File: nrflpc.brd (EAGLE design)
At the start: 67.9 x 38.8 mm, 62 parts, among them IC1 LPC1111/12/13/14-HVQFN33, IC3 LM3401, IC5 LM3401, IC6 LM3401, IC7 LM3401, IC8 78L05SMD, Q1 20MHz, Q2 MOSFET-PCHANNEL, Q3 MOSFET-PCHANNEL, Q4 MOSFET-PCHANNEL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

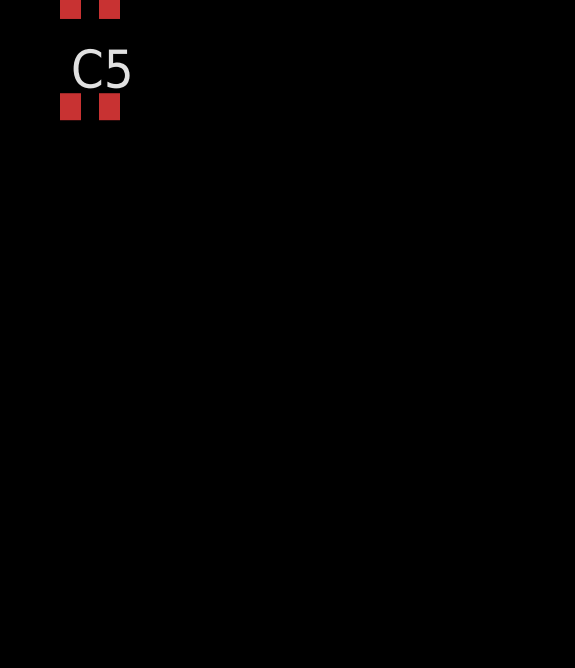
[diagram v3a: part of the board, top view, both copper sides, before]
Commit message: ADC input filters
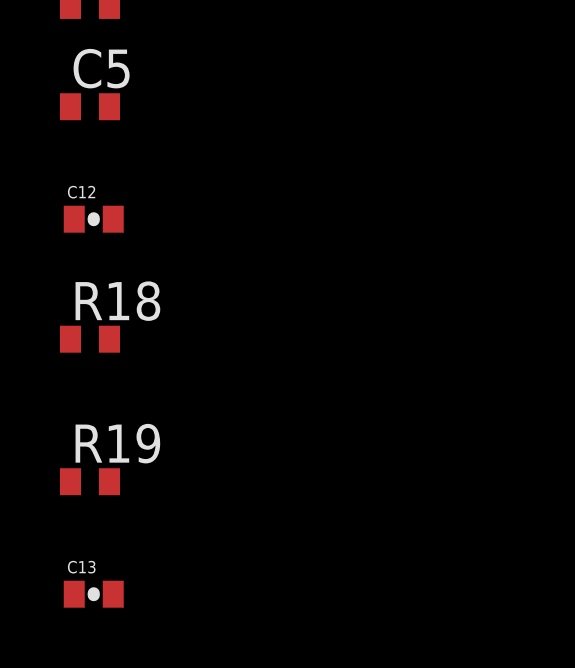
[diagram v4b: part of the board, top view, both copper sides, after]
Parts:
- added C12, C13: 200pF, SparkFun:0402-CAP
- added R18, R19: 4.7k, rcl:R0402
- R1: value (none) -> 100k
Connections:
- removed net AD0: IC1.20
- new net AD6: C13.2, IC1.20, R19.2
- new net AIN0: R18.1
- new net AIN1: R19.1
- net AD1: now also C12.2, R18.2
- net GND: now also C12.1, C13.1
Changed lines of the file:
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@@
 <element name="C3" library="rcl" package="C0402" value="100nF" x="-8.875" y="-15.125"/>
 <element name="C4" library="rcl" package="C0402" value="100nF" x="-8.875" y="-18.5"/>
-<element name="R1" library="rcl" package="R0402" value="" x="-8.875" y="-23.25"/>
+<element name="R1" library="rcl" package="R0402" value="100k" x="-8.875" y="-23.25"/>
 <element name="C5" library="rcl" package="C0402" value="100nF" x="-8.875" y="-26.625"/>
 <element name="PWR" library="pinhead" package="1X02" value="" x="11.375" y="2.75"/>
+<element name="C12" library="SparkFun" package="0402-CAP" value="200pF" x="-8.75" y="-30.375"/>
+<element name="R18" library="rcl" package="R0402" value="4.7k" x="-8.875" y="-34.375"/>
+<element name="C13" library="SparkFun" package="0402-CAP" value="200pF" x="-8.75" y="-42.875"/>
+<element name="R19" library="rcl" package="R0402" value="4.7k" x="-8.875" y="-39.125"/>
 </elements>
 <signals>
@@
 <contactref element="C5" pad="2"/>
 <contactref element="PWR" pad="2"/>
-<wire x1="34.549" y1="19.0205" x2="32.625" y2="8.75" width="0" layer="19" extent="1-1"/>
+<contactref element="C12" pad="1"/>
+<contactref element="C13" pad="1"/>
+<wire x1="52.178" y1="32.8" x2="57.66" y2="33.496" width="0" layer="19" extent="1-1"/>
+<wire x1="50.252" y1="32.743" x2="52.178" y2="32.8" width="0" layer="19" extent="1-1"/>
+<wire x1="49.752" y1="31.143" x2="50.252" y2="32.743" width="0" layer="19" extent="1-1"/>
+<wire x1="48.352" y1="30.743" x2="49.752" y2="31.143" width="0" layer="19" extent="1-1"/>
+<wire x1="48.152" y1="29.243" x2="48.352" y2="30.743" width="0" layer="19" extent="1-1"/>
+<wire x1="49.752" y1="29.343" x2="48.152" y2="29.243" width="0" layer="19" extent="1-1"/>
+<wire x1="49.952" y1="27.643" x2="49.752" y2="29.343" width="0" layer="19" extent="1-1"/>
+<wire x1="51" y1="26.3" x2="49.952" y2="27.643" width="0" layer="19" extent="1-1"/>
+<wire x1="52.4" y1="29.4" x2="49.752" y2="29.343" width="0" layer="19" extent="1-1"/>
+<wire x1="50.64" y1="23.639" x2="51" y2="26.3" width="0" layer="19" extent="1-16"/>
+<wire x1="49.851" y1="22.589" x2="50.64" y2="23.639" width="0" layer="19" extent="16-16"/>
+<wire x1="48.561" y1="22.709" x2="49.851" y2="22.589" width="0" layer="19" extent="1-1"/>
+<wire x1="49.1" y1="20.3" x2="49.851" y2="22.589" width="0" layer="19" extent="1-1"/>
+<wire x1="55.103" y1="17.634" x2="54.025" y2="21.5" width="0" layer="19" extent="1-1"/>
+<wire x1="57.8" y1="18.2" x2="55.103" y2="17.634" width="0" layer="19" extent="1-1"/>
+<wire x1="41.56" y1="33.696" x2="48.352" y2="30.743" width="0" layer="19" extent="1-1"/>
+<wire x1="35.978" y1="32.8" x2="41.56" y2="33.696" width="0" layer="19" extent="1-1"/>
+<wire x1="33.952" y1="32.543" x2="35.978" y2="32.8" width="0" layer="19" extent="1-1"/>
+<wire x1="33.652" y1="30.943" x2="33.952" y2="32.543" width="0" layer="19" extent="1-1"/>
+<wire x1="32.252" y1="30.743" x2="33.652" y2="30.943" width="0" layer="19" extent="1-1"/>
+<wire x1="31.952" y1="29.243" x2="32.252" y2="30.743" width="0" layer="19" extent="1-1"/>
+<wire x1="33.352" y1="29.043" x2="31.952" y2="29.243" width="0" layer="19" extent="1-1"/>
+<wire x1="33.352" y1="27.543" x2="33.352" y2="29.043" width="0" layer="19" extent="1-1"/>
+<wire x1="34.7" y1="26" x2="33.352" y2="27.543" width="0" layer="19" extent="1-1"/>
+<wire x1="36.2" y1="29" x2="33.352" y2="29.043" width="0" layer="19" extent="1-1"/>
+<wire x1="34.609" y1="23" x2="34.7" y2="26" width="0" layer="19" extent="1-16"/>
+<wire x1="32.952" y1="22.643" x2="34.152" y2="22.543" width="0" layer="19" extent="16-16"/>
+<wire x1="31.752" y1="22.643" x2="32.952" y2="22.643" width="0" layer="19" extent="1-1"/>
+<wire x1="32.5" y1="20.2" x2="32.952" y2="22.643" width="0" layer="19" extent="1-1"/>
+<wire x1="34.549" y1="19.0205" x2="32.5" y2="20.2" width="0" layer="19" extent="1-1"/>
+<wire x1="24.76" y1="33.596" x2="32.252" y2="30.743" width="0" layer="19" extent="1-1"/>
+<wire x1="19.278" y1="32.7" x2="24.76" y2="33.596" width="0" layer="19" extent="1-1"/>
+<wire x1="17.352" y1="32.943" x2="19.278" y2="32.7" width="0" layer="19" extent="1-1"/>
+<wire x1="17.152" y1="31.343" x2="17.352" y2="32.943" width="0" layer="19" extent="1-1"/>
+<wire x1="15.852" y1="31.243" x2="17.152" y2="31.343" width="0" layer="19" extent="1-1"/>
+<wire x1="16.952" y1="29.743" x2="17.152" y2="31.343" width="0" layer="19" extent="1-1"/>
+<wire x1="16.952" y1="28.143" x2="16.952" y2="29.743" width="0" layer="19" extent="1-1"/>
+<wire x1="15.352" y1="29.643" x2="16.952" y2="29.743" width="0" layer="19" extent="1-1"/>
+<wire x1="19.7" y1="28.8" x2="16.952" y2="28.143" width="0" layer="19" extent="1-1"/>
+<wire x1="18.3" y1="25.6" x2="16.952" y2="28.143" width="0" layer="19" extent="1-1"/>
+<wire x1="18.109" y1="22.6" x2="18.3" y2="25.6" width="0" layer="19" extent="1-16"/>
+<wire x1="16.852" y1="22.643" x2="18.052" y2="22.543" width="0" layer="19" extent="16-16"/>
+<wire x1="15.552" y1="22.643" x2="16.852" y2="22.643" width="0" layer="19" extent="1-1"/>
+<wire x1="16.2" y1="20.3" x2="15.552" y2="22.643" width="0" layer="19" extent="1-1"/>
+<wire x1="18.349" y1="17.9615" x2="16.2" y2="20.3" width="0" layer="19" extent="1-1"/>
+<wire x1="8.46" y1="33.696" x2="15.852" y2="31.243" width="0" layer="19" extent="1-1"/>
+<wire x1="3.278" y1="32.8" x2="8.46" y2="33.696" width="0" layer="19" extent="1-1"/>
+<wire x1="1.452" y1="32.843" x2="3.278" y2="32.8" width="0" layer="19" extent="1-1"/>
+<wire x1="1.552" y1="31.243" x2="1.452" y2="32.843" width="0" layer="19" extent="1-1"/>
+<wire x1="1.652" y1="34.743" x2="1.452" y2="32.843" width="0" layer="19" extent="1-1"/>
+<wire x1="3.3" y1="29.1" x2="1.552" y2="31.243" width="0" layer="19" extent="1-1"/>
+<wire x1="1.152" y1="27.343" x2="3.3" y2="29.1" width="0" layer="19" extent="1-1"/>
+<wire x1="2.9" y1="26" x2="1.152" y2="27.343" width="0" layer="19" extent="1-1"/>
+<wire x1="5.452" y1="24.143" x2="2.9" y2="26" width="0" layer="19" extent="1-1"/>
+<wire x1="6.725" y1="20.8" x2="5.452" y2="24.143" width="0" layer="19" extent="1-1"/>
+<wire x1="3.849" y1="17.4865" x2="6.852" y2="18.743" width="0" layer="19" extent="1-1"/>
+<wire x1="2.8" y1="12.71" x2="3.849" y2="17.4865" width="0" layer="19" extent="1-1"/>
+<wire x1="9.05" y1="10.985" x2="2.8" y2="12.71" width="0" layer="19" extent="1-1"/>
+<wire x1="9.05" y1="9.715" x2="9.05" y2="10.985" width="0" layer="19" extent="1-1"/>
+<wire x1="9.15" y1="6.75" x2="9.05" y2="9.715" width="0" layer="19" extent="1-1"/>
+<wire x1="12.9" y1="6.75" x2="9.15" y2="6.75" width="0" layer="19" extent="1-1"/>
+<wire x1="14.25" y1="9.715" x2="12.9" y2="6.75" width="0" layer="19" extent="1-1"/>
+<wire x1="14.25" y1="10.985" x2="14.25" y2="9.715" width="0" layer="19" extent="1-1"/>
+<wire x1="12.645" y1="2.75" x2="12.9" y2="6.75" width="0" layer="19" extent="1-1"/>
+<wire x1="65.052" y1="27.143" x2="57.66" y2="33.496" width="0" layer="19" extent="1-1"/>
+<wire x1="32.625" y1="8.75" x2="34.549" y2="19.0205" width="0" layer="19" extent="1-1"/>
+<wire x1="56.02" y1="4.74" x2="55.103" y2="17.634" width="0" layer="19" extent="1-1"/>
 <wire x1="-8.225" y1="-5.625" x2="9.15" y2="6.75" width="0" layer="19" extent="1-1"/>
 <wire x1="-9.525" y1="-10.375" x2="-8.225" y2="-5.625" width="0" layer="19" extent="1-1"/>
@@
 <wire x1="-8.225" y1="-18.5" x2="-8.225" y2="-15.125" width="0" layer="19" extent="1-1"/>
 <wire x1="-8.225" y1="-26.625" x2="-8.225" y2="-18.5" width="0" layer="19" extent="1-1"/>
+<wire x1="-9.4" y1="-30.375" x2="-8.225" y2="-26.625" width="0" layer="19" extent="1-1"/>
+<wire x1="-9.4" y1="-42.875" x2="-9.4" y2="-30.375" width="0" layer="19" extent="1-1"/>
 </signal>
 <signal name="N$1">
@@
 <wire x1="-9.525" y1="-5.625" x2="22.575" y2="9.525" width="0" layer="19" extent="1-1"/>
 </signal>
-<signal name="AD0">
+<signal name="AD6">
 <contactref element="IC1" pad="20"/>
+<contactref element="R19" pad="2"/>
+<contactref element="C13" pad="2"/>
+<wire x1="-8.225" y1="-39.125" x2="-8.1" y2="-42.875" width="0" layer="19" extent="1-1"/>
+<wire x1="36.025" y1="8.425" x2="-8.225" y2="-39.125" width="0" layer="19" extent="1-1"/>
 </signal>
 <signal name="AD1">
 <contactref element="IC1" pad="22"/>
+<contactref element="R18" pad="2"/>
+<contactref element="C12" pad="2"/>
+<wire x1="-8.1" y1="-30.375" x2="36.025" y2="9.725" width="0" layer="19" extent="1-1"/>
+<wire x1="-8.225" y1="-34.375" x2="-8.1" y2="-30.375" width="0" layer="19" extent="1-1"/>
 </signal>
 <signal name="IO0">
@@
 <contactref element="IC1" pad="11"/>
 </signal>
+<signal name="AIN0">
+<contactref element="R18" pad="1"/>
+</signal>
+<signal name="AIN1">
+<contactref element="R19" pad="1"/>
+</signal>
 </signals>

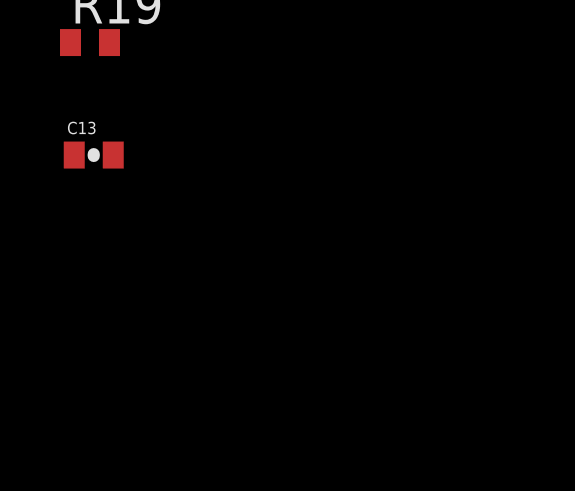
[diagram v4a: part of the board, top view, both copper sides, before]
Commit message: UART series resistors
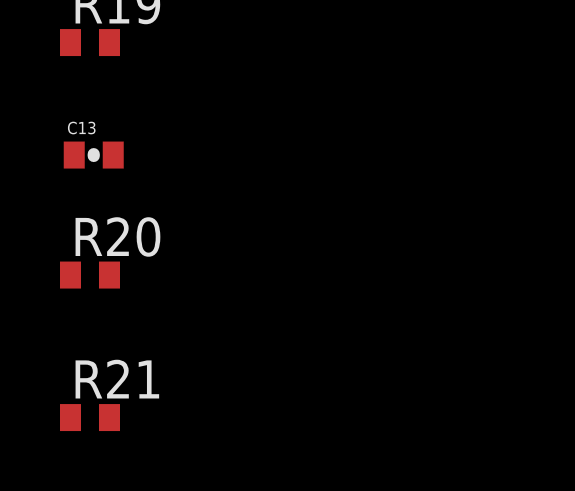
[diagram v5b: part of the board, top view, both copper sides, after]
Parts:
- added R20, R21: 150, rcl:R0402
- R1: value 100k -> 15k
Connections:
- new net N$27: IC1.31, R20.1
- new net N$30: IC1.32, R21.1
- net RXD: now also R20.2; no longer IC1.31
- net TXD: now also R21.2; no longer IC1.32
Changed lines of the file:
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@@
 <element name="C3" library="rcl" package="C0402" value="100nF" x="-8.875" y="-15.125"/>
 <element name="C4" library="rcl" package="C0402" value="100nF" x="-8.875" y="-18.5"/>
-<element name="R1" library="rcl" package="R0402" value="100k" x="-8.875" y="-23.25"/>
+<element name="R1" library="rcl" package="R0402" value="15k" x="-8.875" y="-23.25"/>
 <element name="C5" library="rcl" package="C0402" value="100nF" x="-8.875" y="-26.625"/>
 <element name="PWR" library="pinhead" package="1X02" value="" x="11.375" y="2.75"/>
@@
 <element name="C13" library="SparkFun" package="0402-CAP" value="200pF" x="-8.75" y="-42.875"/>
 <element name="R19" library="rcl" package="R0402" value="4.7k" x="-8.875" y="-39.125"/>
+<element name="R20" library="rcl" package="R0402" value="150" x="-8.875" y="-46.875"/>
+<element name="R21" library="rcl" package="R0402" value="150" x="-8.875" y="-51.625"/>
 </elements>
 <signals>
@@
 <signal name="RXD">
 <contactref element="FTDI" pad="2"/>
-<contactref element="IC1" pad="31"/>
-<wire x1="2.8" y1="7.63" x2="31" y2="12.15" width="0" layer="19" extent="1-1"/>
+<contactref element="R20" pad="2"/>
+<wire x1="2.8" y1="7.63" x2="-8.225" y2="-46.875" width="0" layer="19" extent="1-1"/>
 </signal>
 <signal name="PB">
@@
 <signal name="TXD">
 <contactref element="FTDI" pad="3"/>
-<contactref element="IC1" pad="32"/>
-<wire x1="2.8" y1="10.17" x2="30.35" y2="12.15" width="0" layer="19" extent="1-1"/>
+<contactref element="R21" pad="2"/>
+<wire x1="2.8" y1="10.17" x2="-8.225" y2="-51.625" width="0" layer="19" extent="1-1"/>
 </signal>
 <signal name="GND">
@@
 <contactref element="R19" pad="1"/>
 </signal>
+<signal name="N$27">
+<contactref element="IC1" pad="31"/>
+<contactref element="R20" pad="1"/>
+<wire x1="31" y1="12.15" x2="-9.525" y2="-46.875" width="0" layer="19" extent="1-1"/>
+</signal>
+<signal name="N$30">
+<contactref element="IC1" pad="32"/>
+<contactref element="R21" pad="1"/>
+<wire x1="30.35" y1="12.15" x2="-9.525" y2="-51.625" width="0" layer="19" extent="1-1"/>
+</signal>
 </signals>

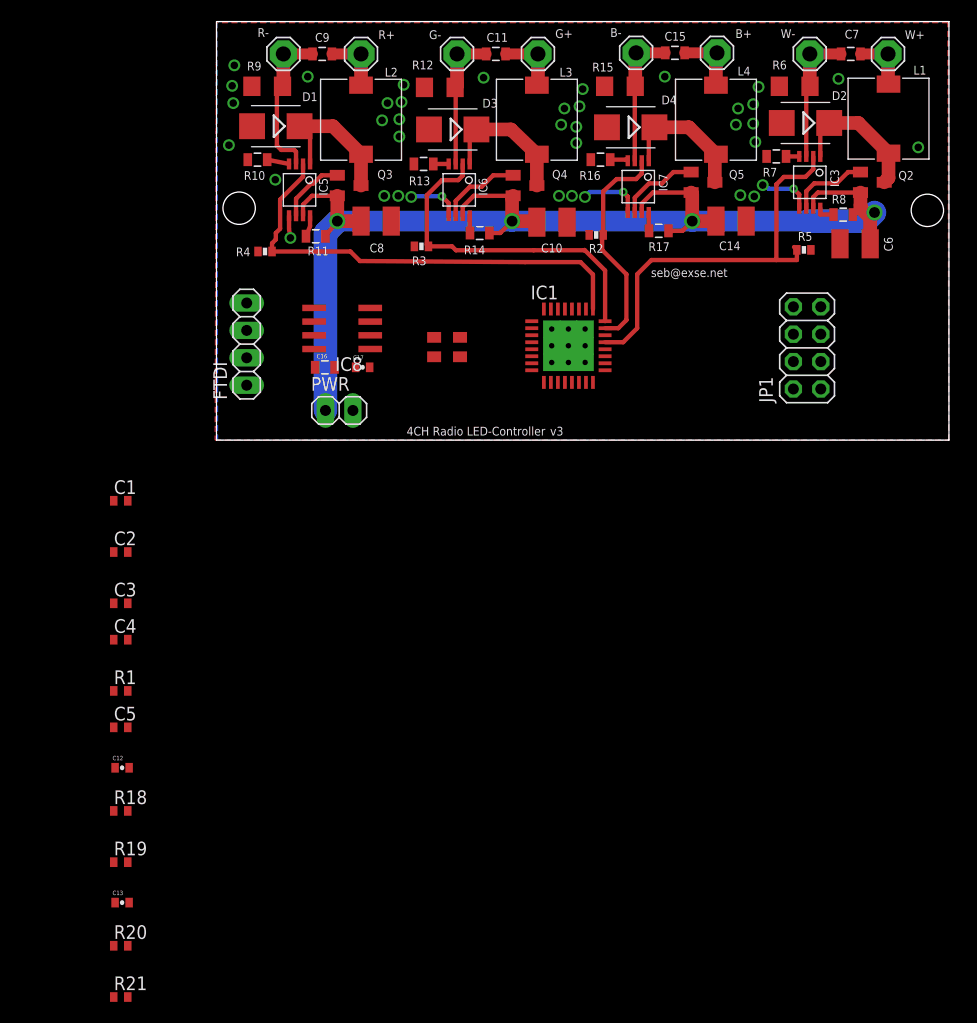
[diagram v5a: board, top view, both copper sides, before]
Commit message: Routing Power supply, in progress
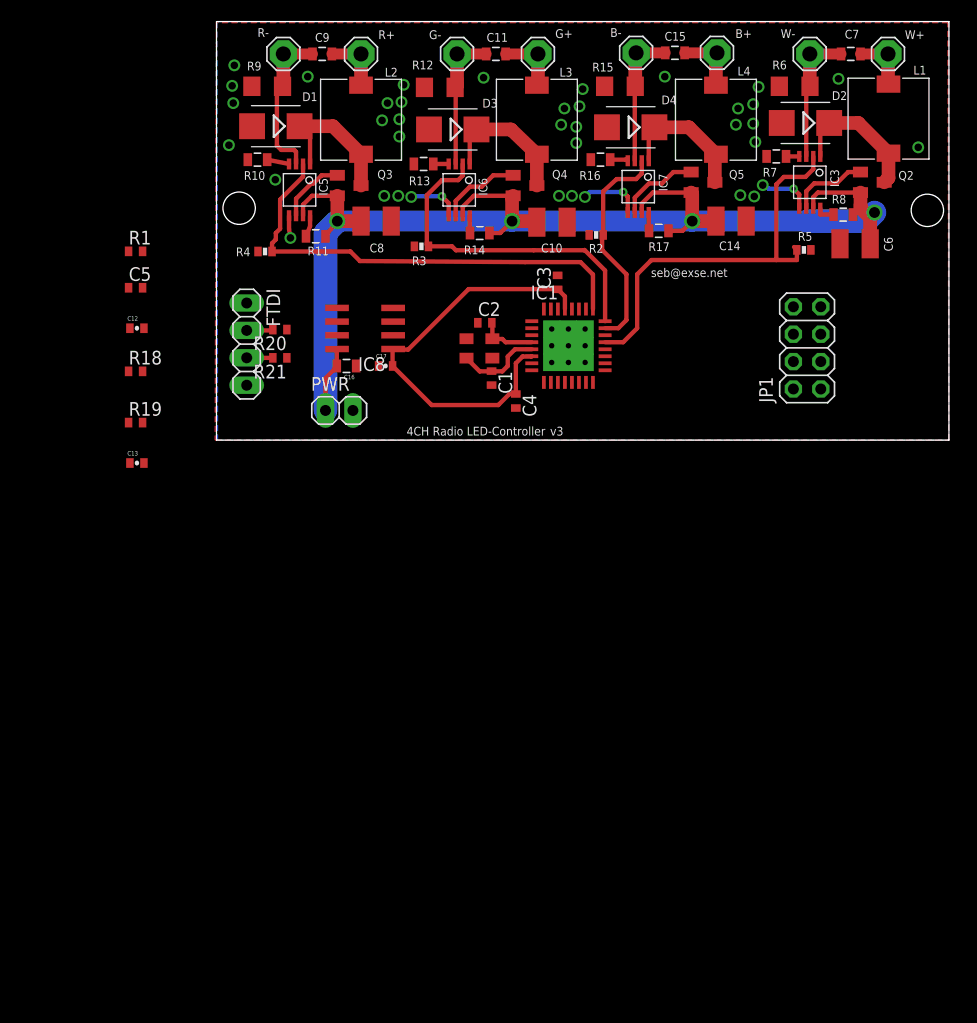
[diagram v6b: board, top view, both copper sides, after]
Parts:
- moved R21 61.1 mm to (5.88, 7.62), turned to 180 degrees
- moved R20 59.0 mm to (5.88, 10.2), turned to 180 degrees
- moved C3 50.3 mm to (31.6, 14.6), turned to 90 degrees
- moved C4 42.8 mm to (27.8, 3.62), turned to 270 degrees
- moved C12 40.8 mm to (-7.38, 10.4)
- moved C13 40.8 mm to (-7.38, -2.12)
- moved C5 40.8 mm to (-7.50, 14.1)
- moved R1 40.8 mm to (-7.50, 17.5)
- moved R18 40.8 mm to (-7.50, 6.38)
- moved R19 40.8 mm to (-7.50, 1.62)
- moved C2 39.9 mm to (24.9, 10.9)
- moved C1 36.2 mm to (25.5, 5.75), turned to 270 degrees
- moved Q1 3.00 mm to (24.4, 8.50), turned to 180 degrees
- moved C17 2.13 mm to (15.7, 6.88)
- moved IC8 2.12 mm to (13.8, 10.3)
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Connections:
- removed net N$18: C16.2, IC8.8
- net +12V: now also C16.2, IC8.8
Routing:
- net +3V3: track 0.00 -> 39.3 mm
- net N$29: track 0.00 -> 8.05 mm
- net +12V: track 118.1 -> 124.2 mm
- net N$19: track 0.00 -> 5.28 mm
- net RXD: track 0.00 -> 2.46 mm
- net TXD: track 0.00 -> 2.43 mm
- net !RST: track 1.04 -> 0.00 mm

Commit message: Layout
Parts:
- added IC2: LT1763CS8-3.3, linear-technology:SOIC8
- added R22: 150, rcl:R0402
- added R23: 15k, rcl:R0402
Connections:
- new net BOOTL: R22.2
- new net N$18: IC1.3, R22.1, R23.1
- net +3V3: now also R23.2
- net GND: now also IC2.3, IC2.6, IC2.7
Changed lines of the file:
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@@
 <element name="R20" library="rcl" package="R0402" value="150" x="5.875" y="10.25" rot="R180"/>
 <element name="R21" library="rcl" package="R0402" value="150" x="5.875" y="7.625" rot="R180"/>
+<element name="IC2" library="linear-technology" package="SOIC8" value="LT1763CS8-3.3" x="-13.5" y="0.125">
+<attribute name="OC_NEWARK" value="57M6055" x="-13.5" y="0.125" size="1.778" layer="27" display="off"/>
+<attribute name="MPN" value="LT1763CS8-3.3" x="-13.5" y="0.125" size="1.778" layer="27" display="off"/>
+<attribute name="MF" value="" x="-13.5" y="0.125" size="1.778" layer="27" display="off"/>
+<attribute name="OC_FARNELL" value="1273617" x="-13.5" y="0.125" size="1.778" layer="27" display="off"/>
+</element>
+<element name="R22" library="rcl" package="R0402" value="150" x="-16.25" y="-6.125"/>
+<element name="R23" library="rcl" package="R0402" value="15k" x="-16.25" y="-10.875"/>
 </elements>
 <signals>
@@
 <contactref element="C12" pad="1"/>
 <contactref element="C13" pad="1"/>
+<contactref element="IC2" pad="3"/>
+<contactref element="IC2" pad="6"/>
+<contactref element="IC2" pad="7"/>
 <wire x1="31.625" y1="15.275" x2="32.625" y2="8.75" width="0" layer="19" extent="1-1"/>
 <wire x1="25.5" y1="5.1" x2="27.75" y2="2.975" width="0" layer="19" extent="1-1"/>
 <wire x1="-6.85" y1="14.125" x2="3.849" y2="17.4865" width="0" layer="19" extent="1-1"/>
 <wire x1="-8.025" y1="10.375" x2="-6.85" y2="14.125" width="0" layer="19" extent="1-1"/>
-<wire x1="-8.025" y1="-2.125" x2="-8.025" y2="10.375" width="0" layer="19" extent="1-1"/>
+<wire x1="-12.865" y1="2.725" x2="-8.025" y2="10.375" width="0" layer="19" extent="1-1"/>
+<wire x1="-14.135" y1="2.725" x2="-12.865" y2="2.725" width="0" layer="19" extent="1-1"/>
+<wire x1="-12.865" y1="-2.475" x2="-12.865" y2="2.725" width="0" layer="19" extent="1-1"/>
+<wire x1="-8.025" y1="-2.125" x2="-12.865" y2="-2.475" width="0" layer="19" extent="1-1"/>
 </signal>
 <signal name="N$1">
@@
 <wire x1="31.625" y1="14" x2="32.3" y2="13.325" width="0.4064" layer="1"/>
 <wire x1="32.3" y1="12.15" x2="32.3" y2="13.325" width="0.4064" layer="1"/>
+<contactref element="R23" pad="2"/>
 <wire x1="32.3" y1="12.15" x2="53.48" y2="4.74" width="0" layer="19" extent="1-1"/>
 <wire x1="31.625" y1="13.975" x2="31.625" y2="14" width="0" layer="19" extent="1-1"/>
 <wire x1="-6.85" y1="17.5" x2="16.325" y2="8.395" width="0" layer="19" extent="1-1"/>
+<wire x1="-15.6" y1="-10.875" x2="-6.85" y2="17.5" width="0" layer="19" extent="1-1"/>
 </signal>
 <signal name="CE">
@@
 <wire x1="6.525" y1="7.625" x2="30.35" y2="12.15" width="0" layer="19" extent="1-1"/>
 </signal>
+<signal name="N$18">
+<contactref element="IC1" pad="3"/>
+<contactref element="R22" pad="1"/>
+<contactref element="R23" pad="1"/>
+<wire x1="-16.9" y1="-6.125" x2="29.225" y2="9.725" width="0" layer="19" extent="1-1"/>
+<wire x1="-16.9" y1="-10.875" x2="-16.9" y2="-6.125" width="0" layer="19" extent="1-1"/>
+</signal>
+<signal name="BOOTL">
+<contactref element="R22" pad="2"/>
+</signal>
 </signals>
